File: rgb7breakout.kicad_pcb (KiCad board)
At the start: 2 copper layers, 26.5 x 49.5 mm, 8 parts, among them J1 RGB7Breakout_Connector, U1 TLC5947RHB

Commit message: set up DRC
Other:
- net class Default: trace_width 0.25 -> 0.2
- net class Power added: clearance 0.2, trace_width 0.5, via_dia 0.6, via_drill 0.4
- rule pad_to_mask_clearance: 0.2 -> 0.0508
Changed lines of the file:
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@@
   )
   (setup
-    (last_trace_width 0.25)
+    (last_trace_width 0.2)
     (trace_clearance 0.2)
     (zone_clearance 0.508)
@@
     (pad_size 1.524 1.524)
     (pad_drill 0.762)
-    (pad_to_mask_clearance 0.2)
+    (pad_to_mask_clearance 0.0508)
     (aux_axis_origin 0 0)
     (visible_elements FFFFF77F)
@@
   (net_class Default "This is the default net class."
     (clearance 0.2)
-    (trace_width 0.25)
+    (trace_width 0.2)
     (via_dia 0.6)
     (via_drill 0.4)
     (uvia_dia 0.3)
     (uvia_drill 0.1)
-    (add_net /VLED)
     (add_net GND)
     (add_net "Net-(D1-Pad1)")
@@
     (add_net VCC)
   )
+  (net_class Power ""
+    (clearance 0.2)
+    (trace_width 0.5)
+    (via_dia 0.6)
+    (via_drill 0.4)
+    (uvia_dia 0.3)
+    (uvia_drill 0.1)
+    (add_net /VLED)
+  )
   (module Capacitors_SMD:CP_Elec_6.3x7.7 (layer B.Cu)

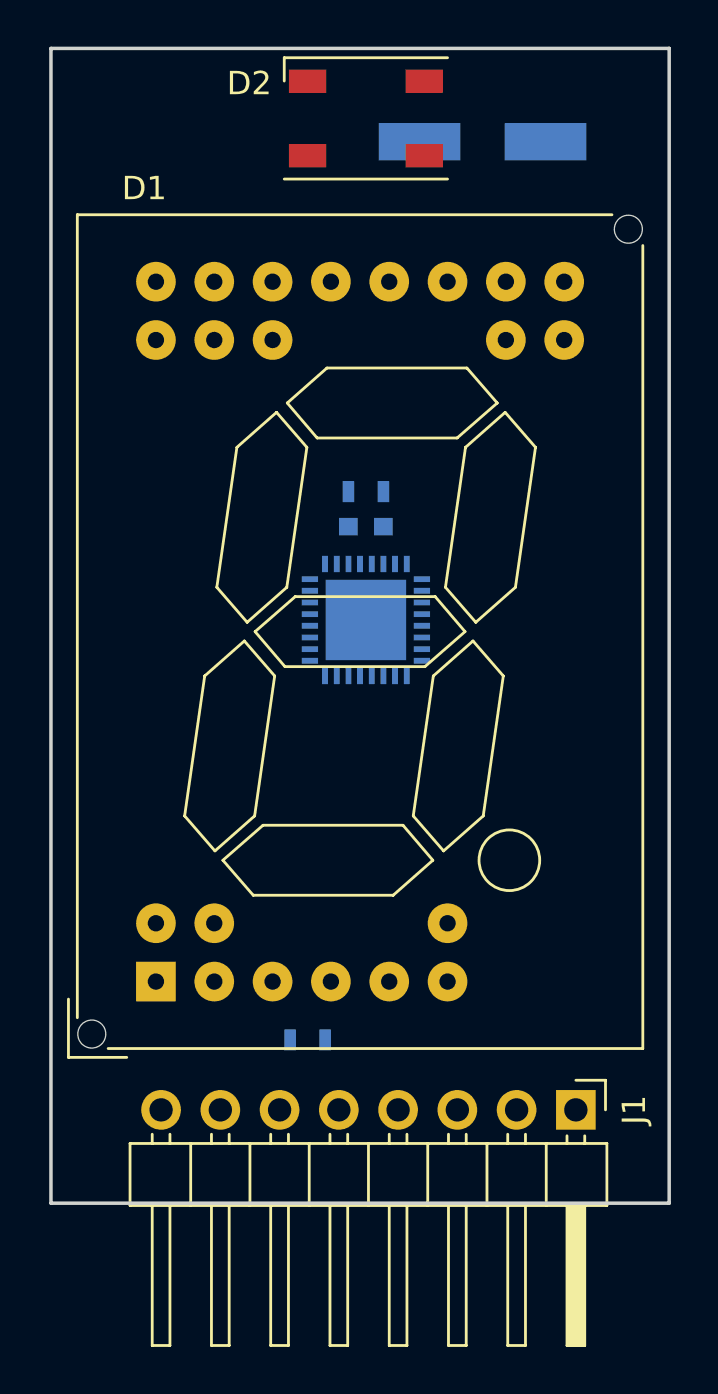
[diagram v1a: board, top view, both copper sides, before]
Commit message: initial placement of HTSSOP and fiducials
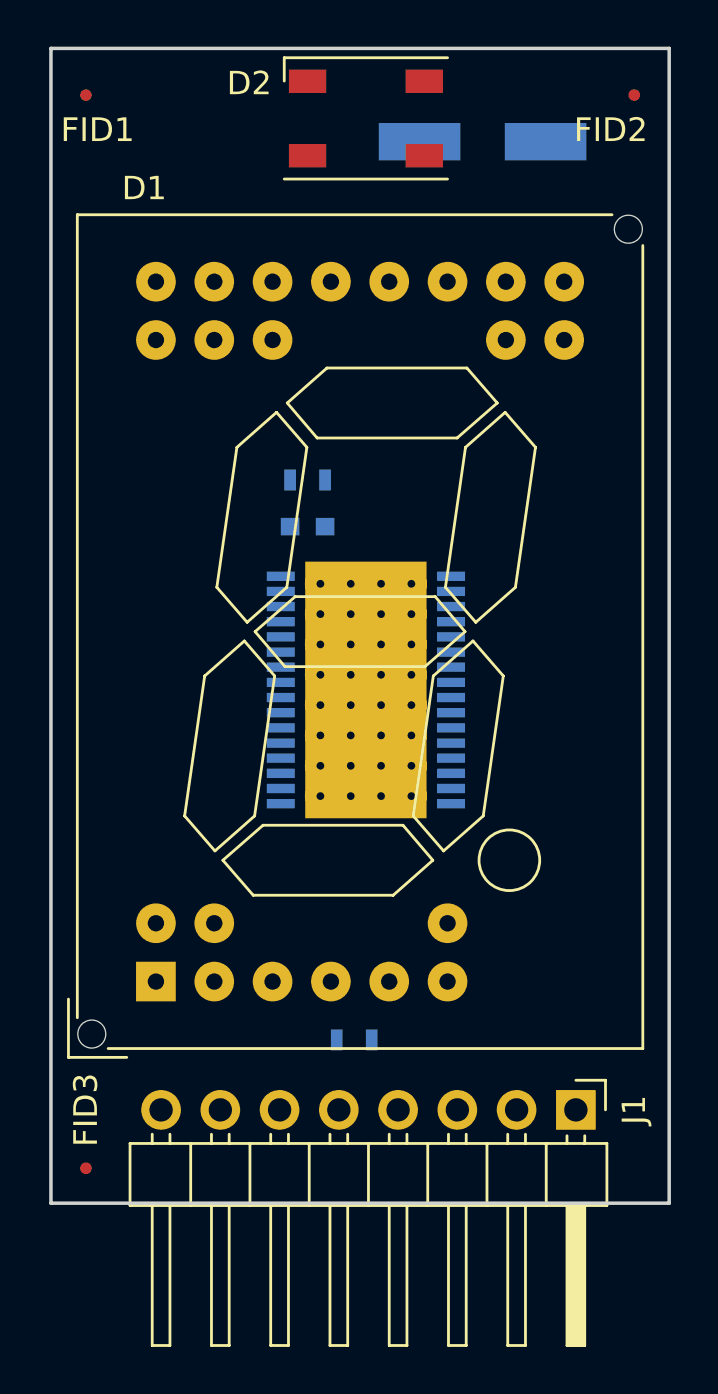
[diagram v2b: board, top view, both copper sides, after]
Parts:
- added FID1: FIDUCIAL_0.5MM, MF_Aesthetics:MF_Aesthetics-FIDUCIAL_0.5MM, F.Cu at (178.0, 78.0)
- added FID2: FIDUCIAL_0.5MM, MF_Aesthetics:MF_Aesthetics-FIDUCIAL_0.5MM, F.Cu at (201.5, 78.0)
- added FID3: FIDUCIAL_0.5MM, MF_Aesthetics:MF_Aesthetics-FIDUCIAL_0.5MM, F.Cu at (178.0, 124.0)
- U1: value TLC5947RHB -> TLC5947DAP; footprint Housings_DFN_QFN:QFN-32-1EP_5x5mm_Pitch0.5mm -> myLibrary:HTSSOP-32_6.1x11mm_Pitch0.65mm_ThermalPad
- moved U1 3.00 mm to (190.0, 103.5)
- moved R1 2.55 mm to (187.5, 94.5)
- moved C2 2.50 mm to (187.5, 96.5)
- moved R2 2.00 mm to (189.5, 118.5)
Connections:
- U1 pad 1: Net-(D1-Pad23) -> GND
- U1 pad 10: Net-(D1-Pad4) -> Net-(D1-Pad24)
- U1 pad 11: Net-(D1-Pad3) -> Net-(D1-Pad6)
- U1 pad 12: Net-(D1-Pad2) -> Net-(D1-Pad11)
- U1 pad 13: Net-(D1-Pad10) -> Net-(D1-Pad5)
- U1 pad 14: Net-(D1-Pad1) -> Net-(D1-Pad4)
- U1 pad 15: Net-(D1-Pad9) -> Net-(D1-Pad3)
- U1 pad 16: Net-(D1-Pad14) -> Net-(D1-Pad2)
- U1 pad 17: Net-(D1-Pad13) -> Net-(D1-Pad10)
- U1 pad 18: Net-(D1-Pad18) -> Net-(D1-Pad1)
- U1 pad 19: Net-(D1-Pad20) -> Net-(D1-Pad9)
- U1 pad 2: Net-(D1-Pad22) -> Net-(J1-Pad5)
- U1 pad 20: Net-(D1-Pad15) -> Net-(D1-Pad14)
- U1 pad 21: Net-(D1-Pad19) -> Net-(D1-Pad13)
- U1 pad 22: Net-(D2-Pad1) -> Net-(D1-Pad18)
- U1 pad 23: Net-(D2-Pad4) -> Net-(D1-Pad20)
- U1 pad 24: Net-(D2-Pad3) -> Net-(D1-Pad15)
- U1 pad 25: Net-(J1-Pad1) -> Net-(D1-Pad19)
- U1 pad 26: Net-(J1-Pad4) -> Net-(D2-Pad1)
- U1 pad 27: Net-(R1-Pad1) -> Net-(D2-Pad4)
- U1 pad 28: VCC -> Net-(D2-Pad3)
- U1 pad 29: GND -> Net-(J1-Pad1)
- U1 pad 3: Net-(D1-Pad21) -> Net-(J1-Pad3)
- U1 pad 30: Net-(J1-Pad5) -> Net-(J1-Pad4)
- U1 pad 31: Net-(J1-Pad3) -> Net-(R1-Pad1)
- U1 pad 32: Net-(J1-Pad2) -> VCC
- U1 pad 4: Net-(D1-Pad25) -> Net-(J1-Pad2)
- U1 pad 5: Net-(D1-Pad16) -> Net-(D1-Pad23)
- U1 pad 6: Net-(D1-Pad24) -> Net-(D1-Pad22)
- U1 pad 7: Net-(D1-Pad6) -> Net-(D1-Pad21)
- U1 pad 8: Net-(D1-Pad11) -> Net-(D1-Pad25)
- U1 pad 9: Net-(D1-Pad5) -> Net-(D1-Pad16)

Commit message: add fiducials on back side of board, too
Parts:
- added FID4: FIDUCIAL_0.5MM, MF_Aesthetics:MF_Aesthetics-FIDUCIAL_0.5MM, B.Cu at (178.0, 78.0)
- added FID5: FIDUCIAL_0.5MM, MF_Aesthetics:MF_Aesthetics-FIDUCIAL_0.5MM, B.Cu at (201.5, 78.0)
- added FID6: FIDUCIAL_0.5MM, MF_Aesthetics:MF_Aesthetics-FIDUCIAL_0.5MM, B.Cu at (178.0, 124.0)
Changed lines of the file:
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@@
     (links 75)
     (no_connects 42)
-    (area 171.72819 74.3456 207.77181 135.489763)
+    (area 176.424999 75.924999 203.075001 125.575001)
     (thickness 1.6)
     (drawings 4)
     (tracks 0)
     (zones 0)
-    (modules 11)
+    (modules 14)
     (nets 34)
   )
@@
     (descr "SMT capacitor, aluminium electrolytic, 6.3x7.7")
     (attr smd)
-    (fp_text reference C1 (at 0 -4.43 180) (layer B.SilkS)
+    (fp_text reference C1 (at 5 2.5 180) (layer B.SilkS)
       (effects (font (size 1 1) (thickness 0.15)) (justify mirror))
     )
@@
     )
   )
+  (module MF_Aesthetics:MF_Aesthetics-FIDUCIAL_0.5MM (layer B.Cu)
+    (at 178 78)
+    (attr smd)
+    (fp_text reference FID4 (at 0.5 1.5) (layer B.SilkS)
+      (effects (font (size 1.016 1.016) (thickness 0.1524)) (justify mirror))
+    )
+    (fp_text value FIDUCIAL_0.5MM (at 0 2.667) (layer B.SilkS) hide
+      (effects (font (size 1.016 1.016) (thickness 0.1524)) (justify mirror))
+    )
+    (pad FID smd circle (at 0 0) (size 0.49784 0.49784) (layers B.Cu B.Paste B.Mask))
+  )
+  (module MF_Aesthetics:MF_Aesthetics-FIDUCIAL_0.5MM (layer B.Cu)
+    (at 201.5 78)
+    (attr smd)
+    (fp_text reference FID5 (at -1 1.5) (layer B.SilkS)
+      (effects (font (size 1.016 1.016) (thickness 0.1524)) (justify mirror))
+    )
+    (fp_text value FIDUCIAL_0.5MM (at 0 2.667) (layer B.SilkS) hide
+      (effects (font (size 1.016 1.016) (thickness 0.1524)) (justify mirror))
+    )
+    (pad FID smd circle (at 0 0) (size 0.49784 0.49784) (layers B.Cu B.Paste B.Mask))
+  )
+  (module MF_Aesthetics:MF_Aesthetics-FIDUCIAL_0.5MM (layer B.Cu)
+    (at 178 124)
+    (attr smd)
+    (fp_text reference FID6 (at 0 -2.5 90) (layer B.SilkS)
+      (effects (font (size 1.016 1.016) (thickness 0.1524)) (justify mirror))
+    )
+    (fp_text value FIDUCIAL_0.5MM (at 0 2.667) (layer B.SilkS) hide
+      (effects (font (size 1.016 1.016) (thickness 0.1524)) (justify mirror))
+    )
+    (pad FID smd circle (at 0 0) (size 0.49784 0.49784) (layers B.Cu B.Paste B.Mask))
+  )
   (gr_line (start 203 125.5) (end 203 76) (angle 90) (layer Edge.Cuts) (width 0.15))

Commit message: routed most of the LED tracks
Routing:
- net Net-(J1-Pad5): track 0.00 -> 38.8 mm, vias 0 -> 2
- net Net-(D1-Pad22): track 0.00 -> 30.4 mm, vias 0 -> 3
- net Net-(J1-Pad3): track 0.00 -> 30.2 mm, vias 0 -> 2
- net Net-(D1-Pad21): track 0.00 -> 29.3 mm, vias 0 -> 3
- net Net-(D1-Pad18): track 0.00 -> 27.2 mm, vias 0 -> 1
- net Net-(J1-Pad2): track 0.00 -> 26.8 mm, vias 0 -> 1
- net Net-(D1-Pad25): track 0.00 -> 25.0 mm, vias 0 -> 1
- net Net-(D1-Pad6): track 0.00 -> 24.3 mm, vias 0 -> 2
- net Net-(D1-Pad24): track 0.00 -> 23.1 mm, vias 0 -> 1
- net Net-(D1-Pad13): track 0.00 -> 22.6 mm, vias 0 -> 1
- net Net-(D1-Pad19): track 0.00 -> 22.0 mm, vias 0 -> 1
- net Net-(D1-Pad2): track 0.00 -> 22.0 mm, vias 0 -> 2
- net Net-(D1-Pad20): track 0.00 -> 21.4 mm, vias 0 -> 1
- net Net-(D1-Pad4): track 0.00 -> 21.1 mm, vias 0 -> 3
- net Net-(D1-Pad23): track 0.00 -> 21.0 mm, vias 0 -> 3
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
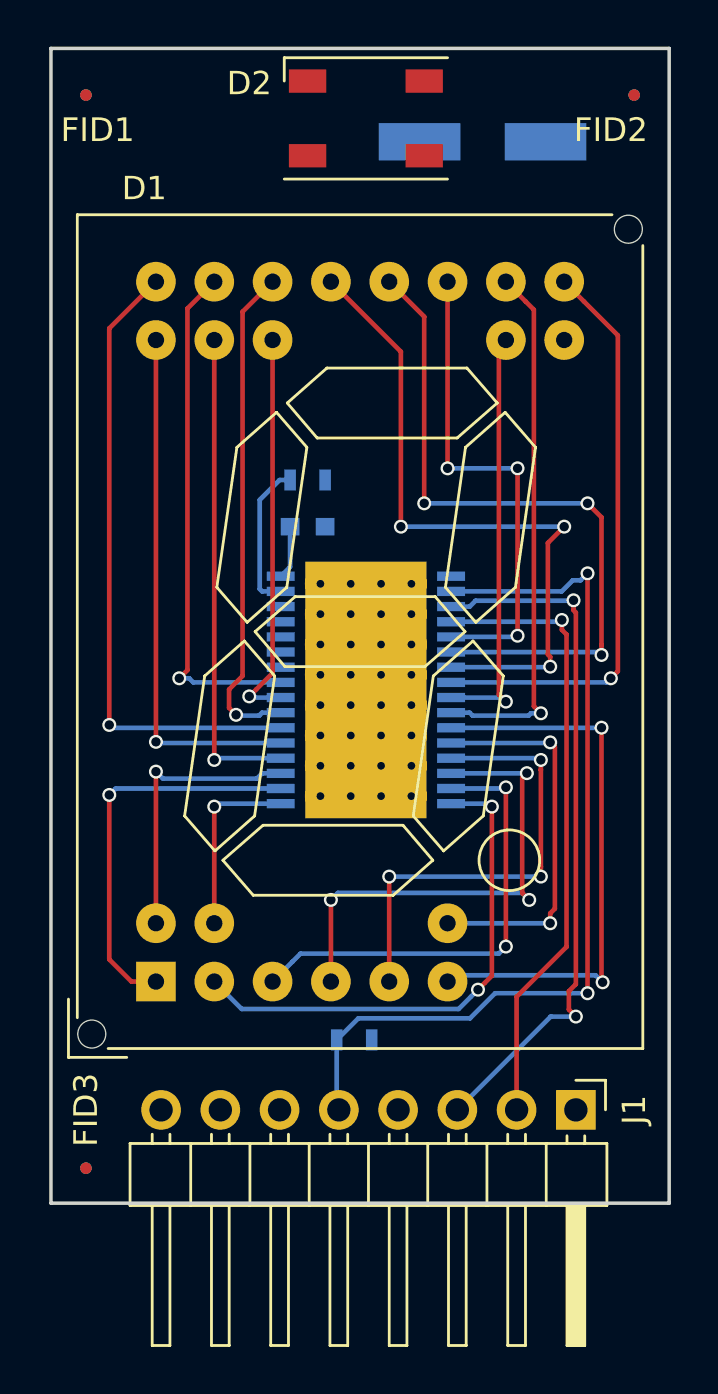
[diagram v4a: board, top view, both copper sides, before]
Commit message: routed more LED tracks
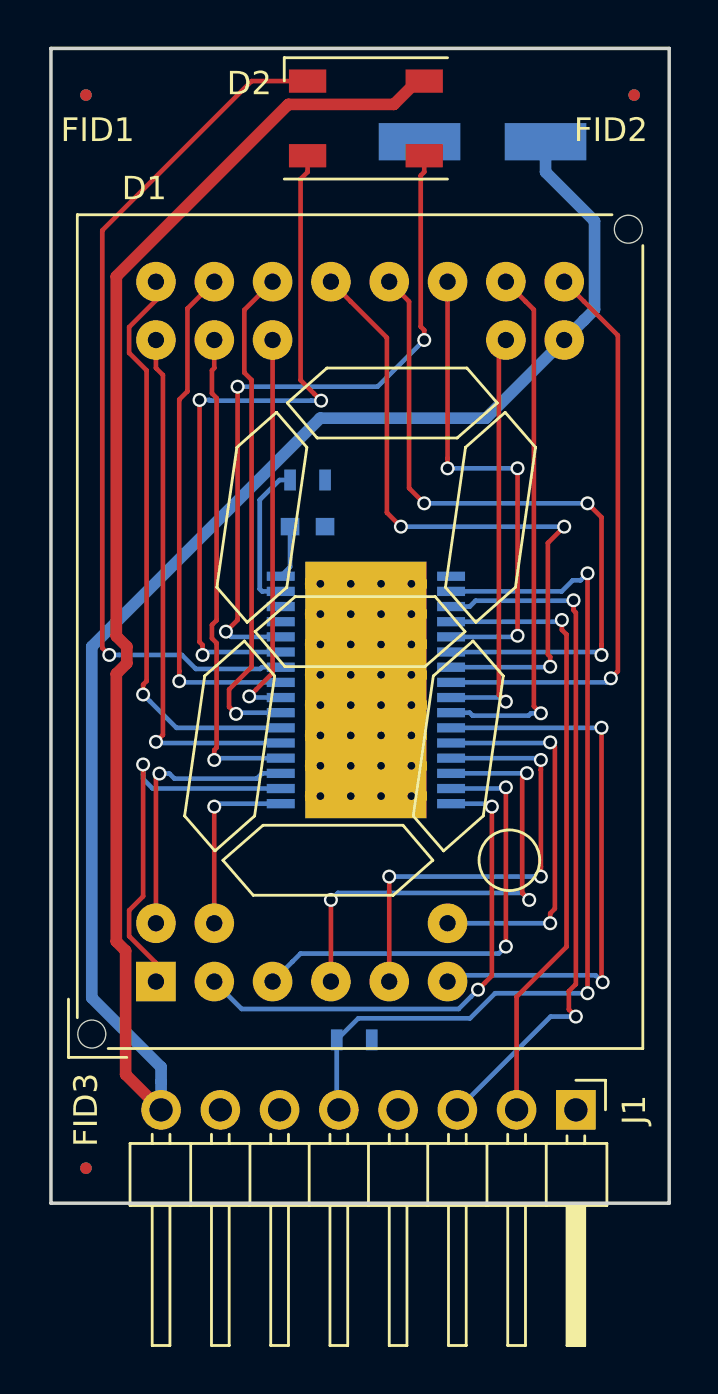
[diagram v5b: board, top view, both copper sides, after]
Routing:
- net /VLED: track 0.00 -> 110.3 mm
- net Net-(D2-Pad1): track 0.00 -> 37.4 mm, vias 0 -> 1
- net Net-(D2-Pad4): track 0.00 -> 30.6 mm, vias 0 -> 3
- net Net-(D2-Pad3): track 0.00 -> 30.0 mm, vias 0 -> 3
- net Net-(D1-Pad18): track 27.2 -> 25.0 mm

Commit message: finished routing all tracks
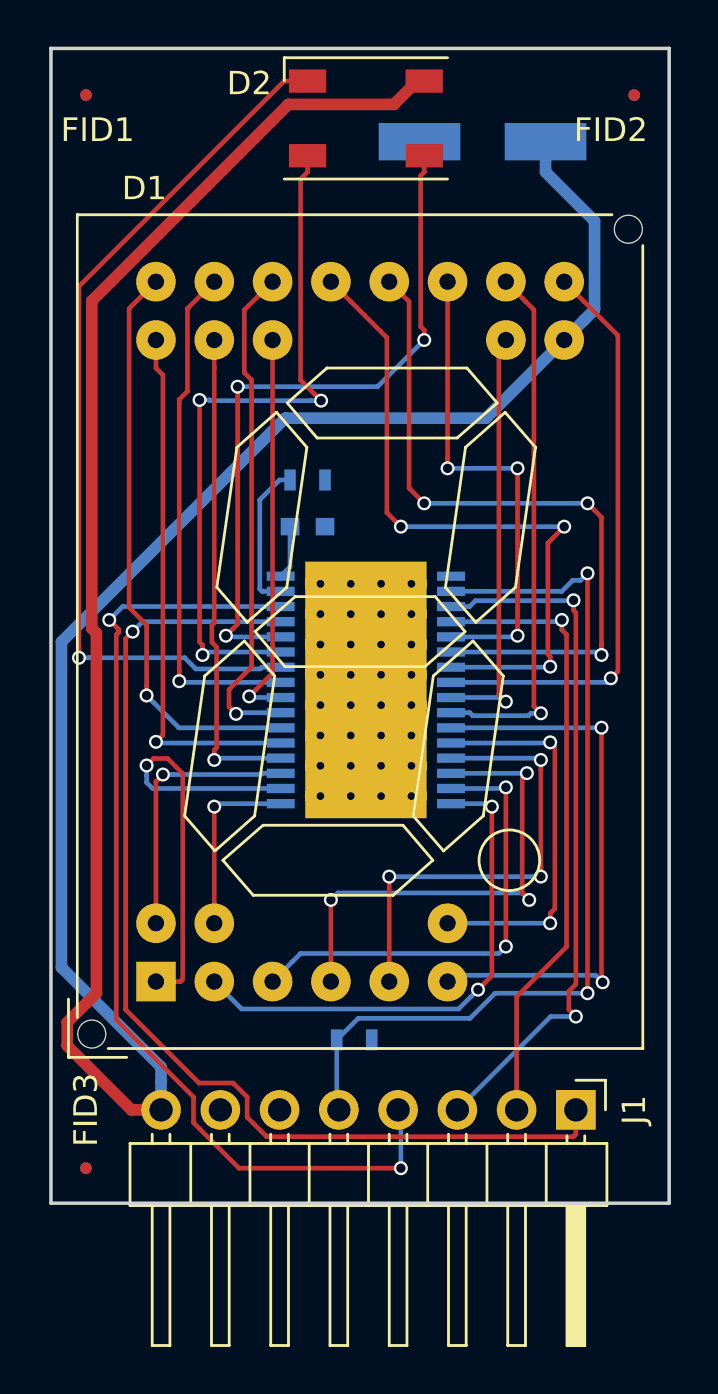
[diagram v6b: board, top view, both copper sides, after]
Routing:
- net Net-(J1-Pad1): track 0.00 -> 46.0 mm, vias 0 -> 1
- net Net-(J1-Pad4): track 0.00 -> 43.0 mm, vias 0 -> 2
- net /VLED: track 110.3 -> 114.5 mm
- net Net-(D1-Pad1): track 16.7 -> 18.5 mm
- net Net-(D2-Pad1): track 37.4 -> 38.2 mm

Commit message: added ground planes on both sides
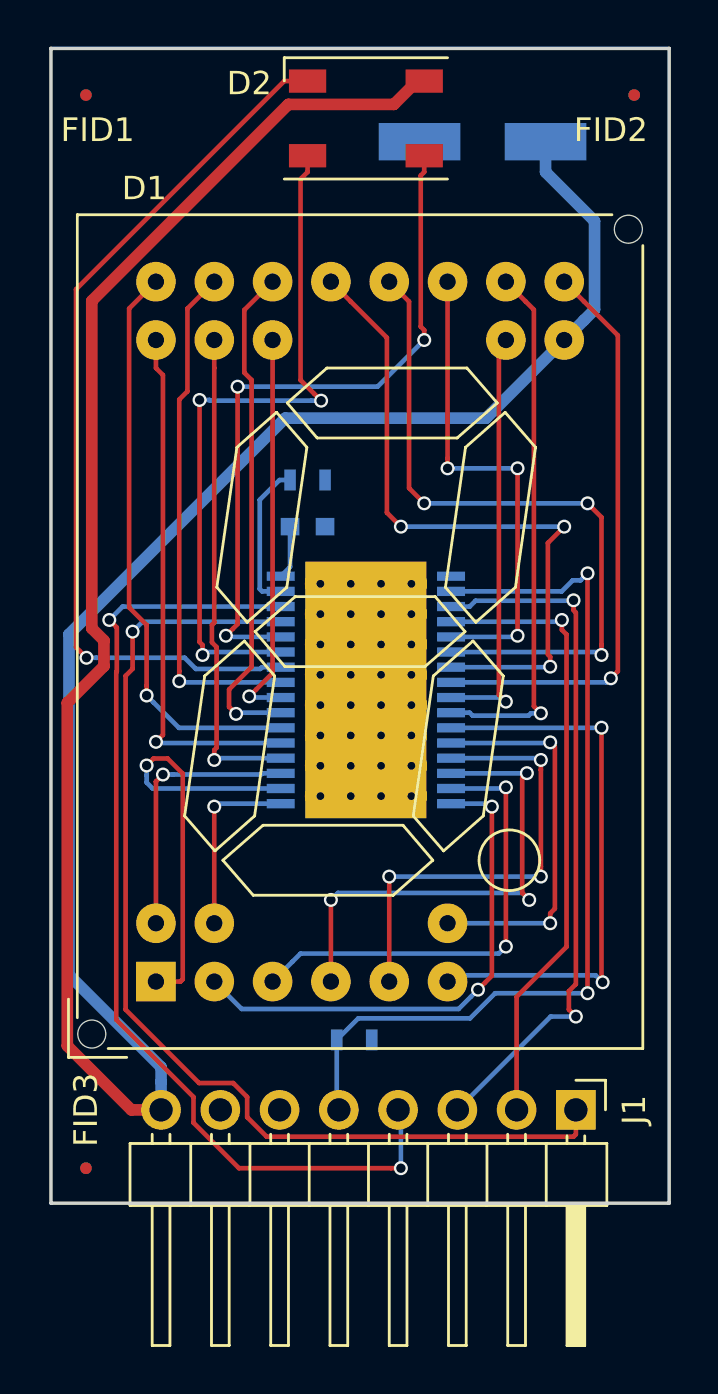
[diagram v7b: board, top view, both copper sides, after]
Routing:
- added copper zone on B.Cu, net GND
- added copper zone on F.Cu, net GND

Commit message: forgot to route VCC
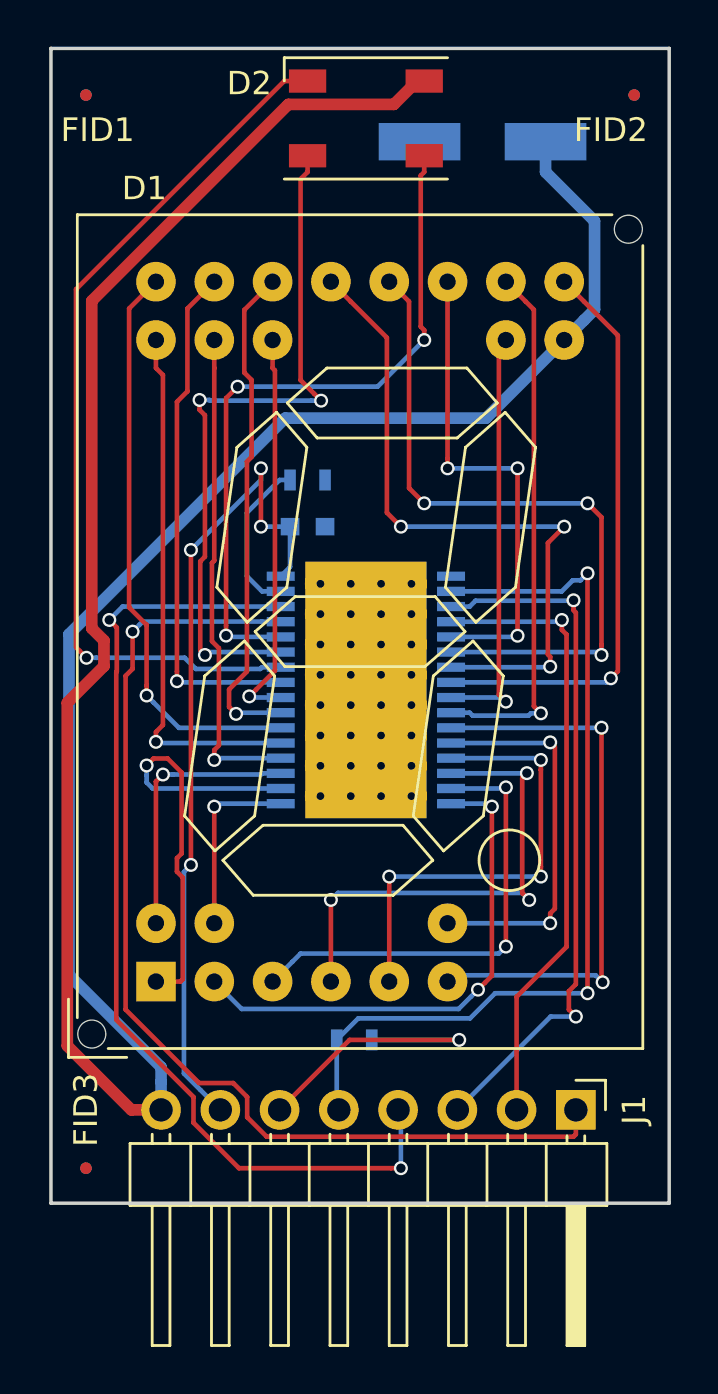
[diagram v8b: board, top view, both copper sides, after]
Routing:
- net VCC: track 2.29 -> 35.6 mm, vias 0 -> 4
- net GND: track 0.00 -> 12.7 mm, vias 0 -> 1
